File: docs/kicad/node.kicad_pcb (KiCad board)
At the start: 2 copper layers, 9 parts, among them U1 ESP32-DevKitC, U2 ESP32-DevKitC, U3 ESP32-DevKitC, U4 ESP32-DevKitC

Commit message: Docs: refactor USB
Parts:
- moved U3 53.3 mm to (117.9, 58.8)
- moved U2 52.2 mm to (43.3, 103.6)
- moved JP1 51.9 mm to (52.8, 89.2)
- moved JP2 51.8 mm to (117.2, 121.3), turned to 0 degrees
- moved JP9 46.9 mm to (111.7, 122.3), turned to 180 degrees
- moved JP8 44.2 mm to (106.7, 122.3), turned to 180 degrees
- moved JP7 43.1 mm to (101.7, 122.3), turned to 180 degrees
- moved U1 34.7 mm to (86.1, 177.7)
- moved U4 16.9 mm to (160.5, 133.7)
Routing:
- net /B3_SCLK: track 43.6 -> 90.1 mm
- net /B1_SCLK: track 40.8 -> 86.5 mm
- net /B1_MOSI: track 25.8 -> 66.3 mm
- net GND: track 230.5 -> 267.6 mm
- net /B5_SCLK: track 53.2 -> 89.9 mm
- net /VCC: track 465.3 -> 500.0 mm
- net /B5_MOSI: track 44.2 -> 78.7 mm
- net /B2_SCLK: track 54.2 -> 84.1 mm
- net /B3_MOSI: track 27.1 -> 56.4 mm
- net /B3_CS: track 24.8 -> 50.7 mm
- net /B1_CS: track 23.8 -> 48.4 mm
- net /B2_MOSI: track 39.3 -> 63.6 mm
- net /B2_CS: track 36.3 -> 49.7 mm
- net /B4_SCLK: track 39.7 -> 34.1 mm
- net /B4_CS: track 38.1 -> 42.2 mm
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
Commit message: Docs: update kicad
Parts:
- added JP3: Jumper_2_Open, Connector_PinSocket_1.00mm:PinSocket_1x02_P1.00mm_Vertical, F.Cu at (180.3, 74.0)
- added JP4: Jumper_2_Open, Connector_PinSocket_1.00mm:PinSocket_1x02_P1.00mm_Vertical, F.Cu at (183.9, 74.0)
- added JP5: Jumper_2_Open, Connector_PinSocket_1.00mm:PinSocket_1x02_P1.00mm_Vertical, F.Cu at (187.4, 74.0)
- added JP6: Jumper_2_Open, Connector_PinSocket_1.00mm:PinSocket_1x02_P1.00mm_Vertical, F.Cu at (191.0, 74.0)
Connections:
- U3 pad 16: /B2_MOSI -> unconnected-(U3-SD_DATA2/GPIO9-Pad16)
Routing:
- net GND: track 267.6 -> 237.9 mm
- net /B5_SCLK: track 89.9 -> 77.5 mm
- net /VCC: track 500.0 -> 487.6 mm
- net /B1_SCLK: track 86.5 -> 74.7 mm
- net /B1_MOSI: track 66.3 -> 57.0 mm
- net /B2_SCLK: track 84.1 -> 77.1 mm
- net /B3_SCLK: track 90.1 -> 83.3 mm
- net /B2_MOSI: track 63.6 -> 58.2 mm
- net /B3_CS: track 50.7 -> 46.7 mm
- net /B5_CS: track 42.3 -> 38.8 mm
- net /B4_CS: track 42.2 -> 38.7 mm
- net /B4_SCLK: track 34.1 -> 31.4 mm
- net /B5_MOSI: track 78.7 -> 76.5 mm
- net /B4_MOSI: track 30.8 -> 29.5 mm
- net /B1_CS: track 48.4 -> 47.2 mm

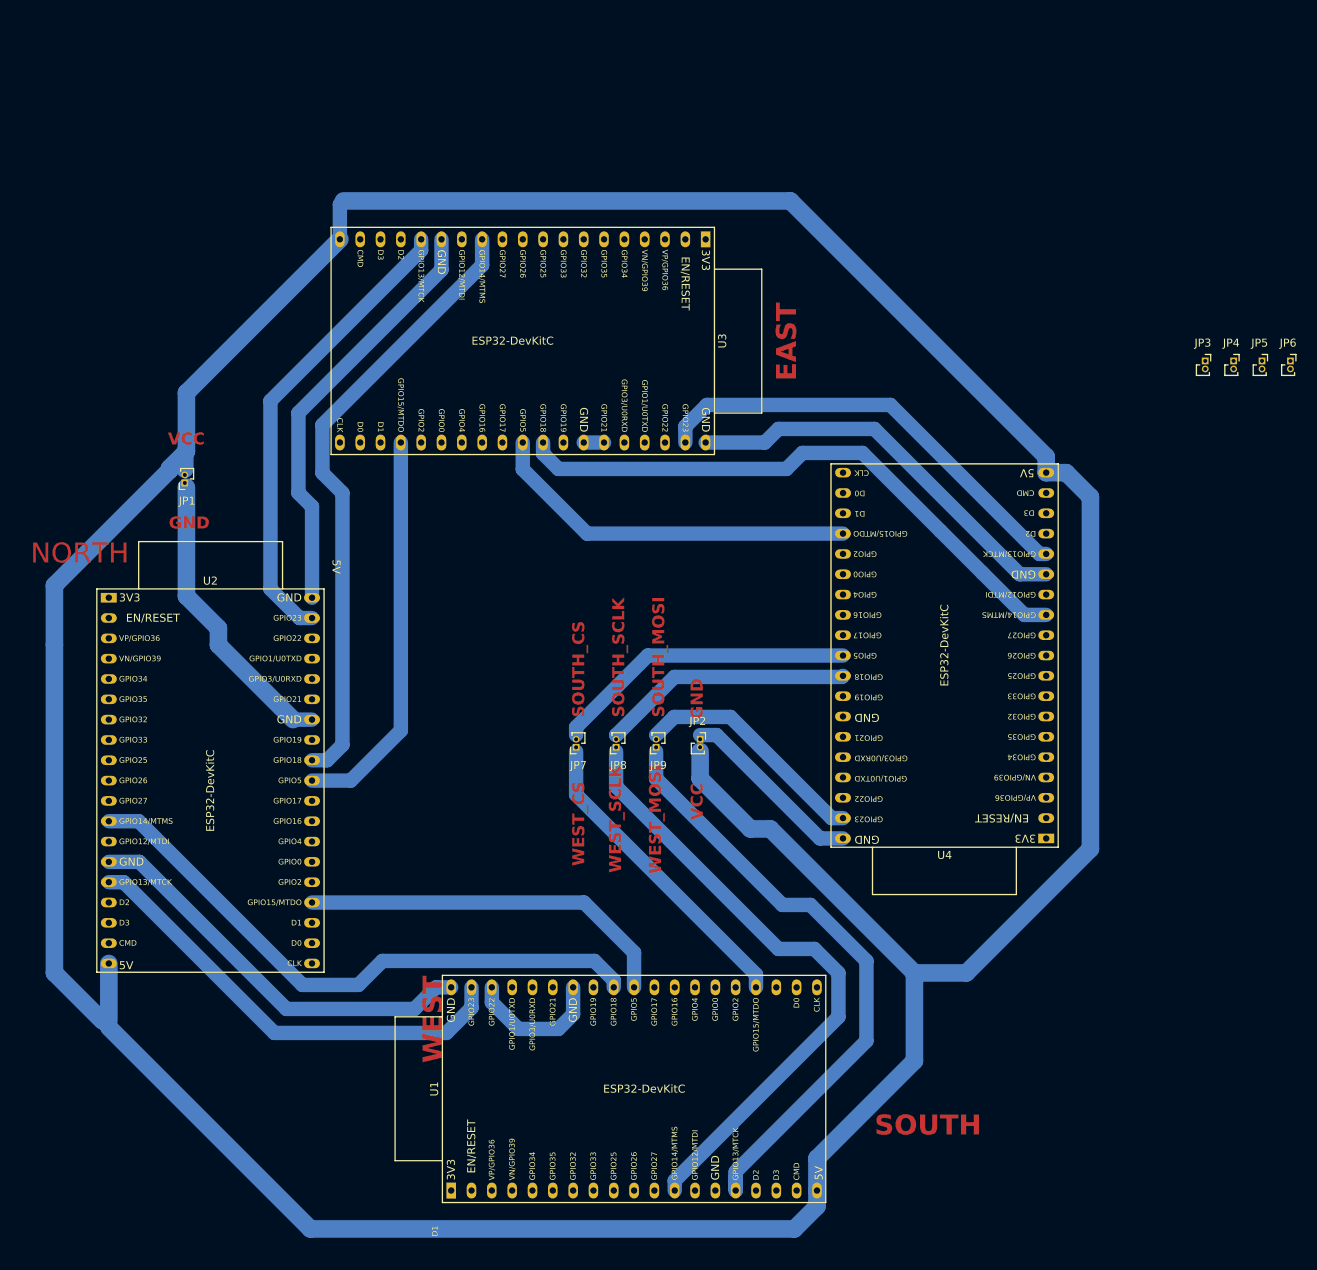
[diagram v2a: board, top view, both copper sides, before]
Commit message: Docs: update kicad - reduce track width to 0.6mm
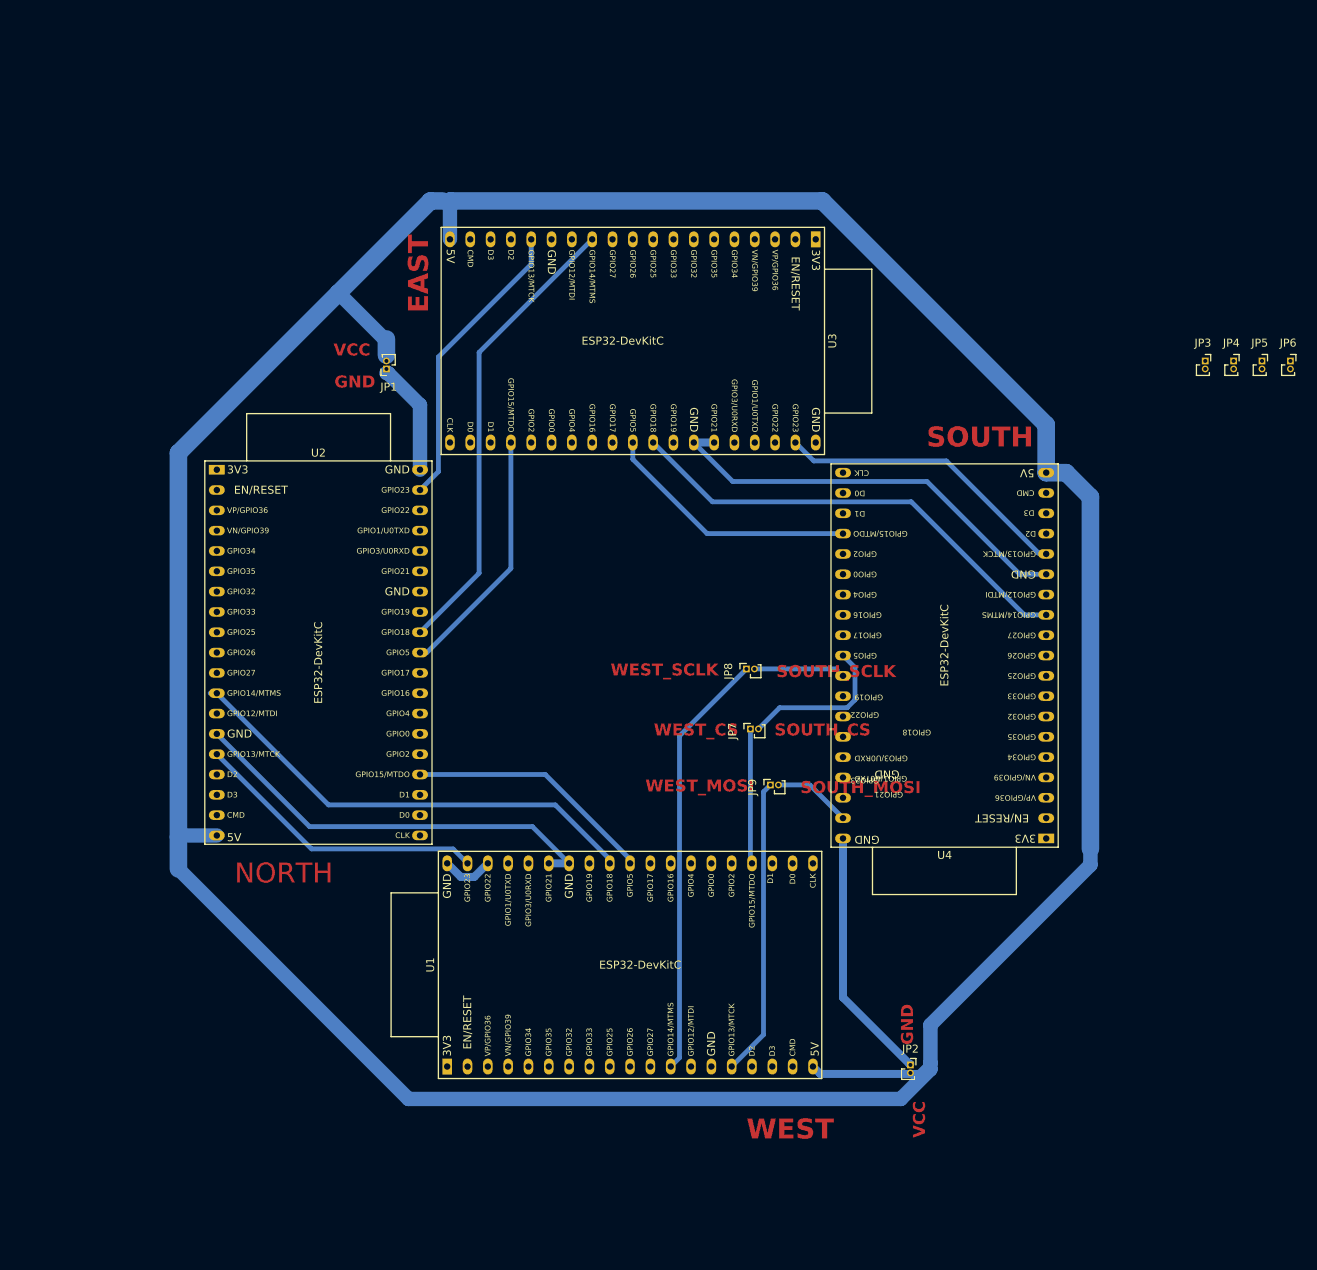
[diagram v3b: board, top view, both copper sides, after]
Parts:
- moved JP2 48.5 mm to (143.5, 162.0)
- moved JP1 29.0 mm to (78.0, 75.0)
- moved JP7 21.9 mm to (123.5, 120.0), turned to 90 degrees
- moved U2 20.9 mm to (56.8, 87.6)
- moved JP8 19.0 mm to (123.0, 112.5), turned to 90 degrees
- moved U1 15.5 mm to (85.6, 162.2)
- moved JP9 15.0 mm to (126.0, 127.0), turned to 90 degrees
- moved U3 13.8 mm to (131.7, 58.8)
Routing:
- net GND: track 237.9 -> 158.9 mm
- net /VCC: track 487.6 -> 419.9 mm
- net /B5_MOSI: track 76.5 -> 37.2 mm
- net /B3_SCLK: track 83.3 -> 58.1 mm
- net /B5_SCLK: track 77.5 -> 53.6 mm
- net /B5_CS: track 38.8 -> 16.9 mm
- net /B2_MOSI: track 58.2 -> 37.1 mm
- net /B4_SCLK: track 31.4 -> 10.4 mm
- net /B4_MOSI: track 29.5 -> 9.79 mm
- net /B1_MOSI: track 57.0 -> 37.5 mm
- net /B2_SCLK: track 77.1 -> 58.0 mm
- net /B4_CS: track 38.7 -> 19.7 mm
- net /B3_MOSI: track 55.9 -> 37.3 mm
- net /B2_CS: track 49.7 -> 31.5 mm
- net /B1_CS: track 47.2 -> 30.6 mm
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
